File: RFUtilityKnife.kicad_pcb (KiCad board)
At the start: 2 copper layers, 100 x 100 mm, 269 parts, among them J1 Conn_01x01, J10 Conn_01x01, J100 Conn_01x01, J101 Conn_01x01, J11 Conn_01x01, J12 Conn_01x01, J126 Conn_Coaxial, J127 Conn_Coaxial, J128 Conn_01x01, J129 Conn_01x01, J13 Conn_01x01, J130 Conn_01x01, J131 Conn_01x01, J14 Conn_01x01, J15 Conn_01x01, J16 Conn_01x01, J17 Conn_01x01, J18 Conn_Coaxial, J2 Barrel_Jack, J22 Barrel_Jack, J23 Barrel_Jack, J24 Conn_Coaxial, J25 Conn_Coaxial, J26 Conn_01x01, J27 Conn_01x01, J28 Conn_01x01, J29 Conn_01x01, J3 Conn_Coaxial, J30 Conn_01x01, J31 Conn_01x01, J32 Conn_01x01, J33 Conn_01x01, J44 Conn_01x01, J45 Conn_01x01, J48 Conn_01x01, J49 Conn_01x01, J5 Conn_01x01, J53 Conn_01x01, J59 Conn_01x01, J6 Conn_01x01, J60 Conn_01x01, J63 Conn_01x01, J65 Conn_01x01, J7 Conn_01x01, J70 Conn_01x01, J71 Conn_01x01, J72 Conn_01x01, J8 Conn_01x01, J9 Conn_01x01, J93 Conn_Coaxial, J95 Conn_Coaxial, J96 Conn_Coaxial, J98 Conn_01x01, J99 Conn_01x01, Q1 BFP740, Q10 BFP740, Q11 BFP740, Q12 BFP740, Q13 BFP740, Q14 BFP740, Q15 BFP740, Q16 BFP740, Q17 BFP740, Q18 BFP740, Q19 BFP740, Q2 BFP740, Q23 BFP740, Q24 MMBT5551, Q25 MMBT5551, Q26 BFP740, Q27 BFP740, Q28 BFP740, Q3 BFP740, Q4 BFP740, Q5 BFP740, Q6 BFP740, Q7 BFP740, Q9 BFP740, U1 KA78M05_TO252, U2 NE555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

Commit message: Cleaned up the layout
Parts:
- C13: value 10 nF -> 1 nF
- C50, C51, C52: value 15 pF -> 1 pF
- R10, R106, R22, R31, R80, R90: value 22R -> 47R
- R105, R29, R9: value 22R -> 10R
- R2, R43, R44: value 22R -> 100R
- moved C11 17.4 mm to (119.6, 71.5)
- moved JP5 13.4 mm to (109.9, 91.7), turned to 180 degrees
- moved U1 8.40 mm to (118.4, 78.1)
- moved J2 8.27 mm to (111.1, 76.5)
- moved C23 7.58 mm to (116.8, 85.9)
- moved C64 7.57 mm to (116.8, 87.9)
- moved C10 7.21 mm to (113.1, 88.5)
- moved R72 6.87 mm to (73.6, 113.5)
- moved R70 5.81 mm to (72.5, 113.5), turned to 270 degrees
- moved R41 3.41 mm to (73.1, 111.7), turned to 90 degrees
- moved R34 3.23 mm to (144.0, 89.9), turned to 180 degrees
- moved R68 2.95 mm to (150.2, 114.3), turned to 270 degrees
- moved R66 2.95 mm to (149.1, 114.3), turned to 270 degrees
- moved C7 2.66 mm to (144.1, 46.2), turned to 180 degrees
- moved C44 2.63 mm to (70.5, 122.4)
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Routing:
- net GND: track 841.1 -> 987.7 mm, vias 370 -> 454
- net Net-(C16-Pad2): track 75.0 -> 62.5 mm
- net NOISEPOWER: track 119.5 -> 107.8 mm
- net Net-(C10-Pad2): track 24.8 -> 15.7 mm
- net Net-(C39-Pad2): track 11.4 -> 4.74 mm
- net MIXERVCC: track 50.8 -> 54.8 mm
- net Net-(Q16-Pad3): track 8.63 -> 4.70 mm
- net Net-(C38-Pad2): track 5.37 -> 7.62 mm
- net +BATT: track 47.6 -> 49.6 mm
- net Net-(C14-Pad2): track 6.68 -> 8.44 mm
- net Net-(C44-Pad2): track 5.61 -> 7.36 mm
- net HIGHVOLTAGE: track 68.0 -> 69.7 mm
- net Net-(J100-Pad1): track 16.6 -> 15.1 mm
- net Net-(C2-Pad2): track 5.48 -> 6.80 mm
- net Net-(C66-Pad1): track 9.01 -> 10.3 mm
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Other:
- board text added: "NE555"
- board text removed: "LM555"

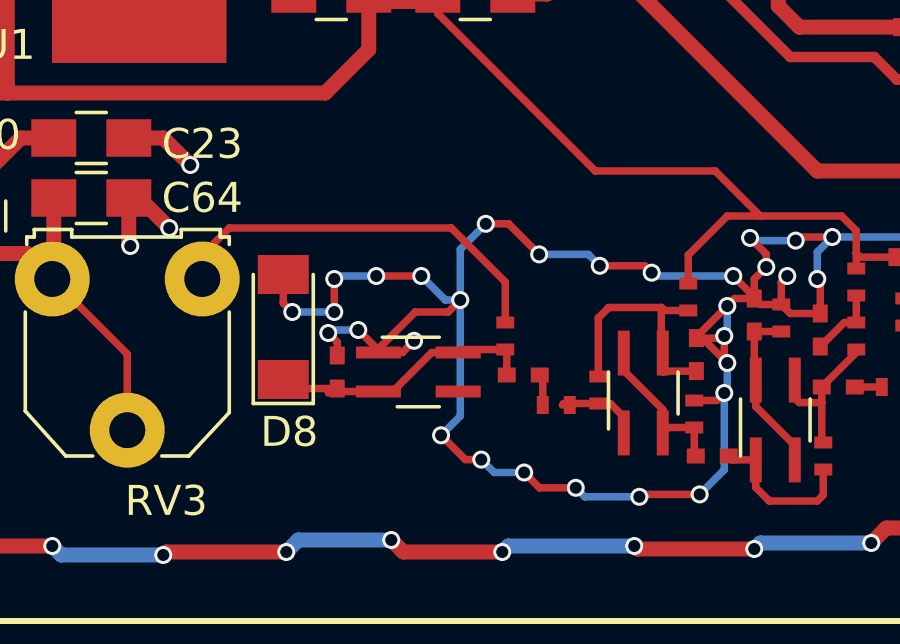
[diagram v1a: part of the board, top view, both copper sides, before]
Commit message: Added vias and changed cut lines
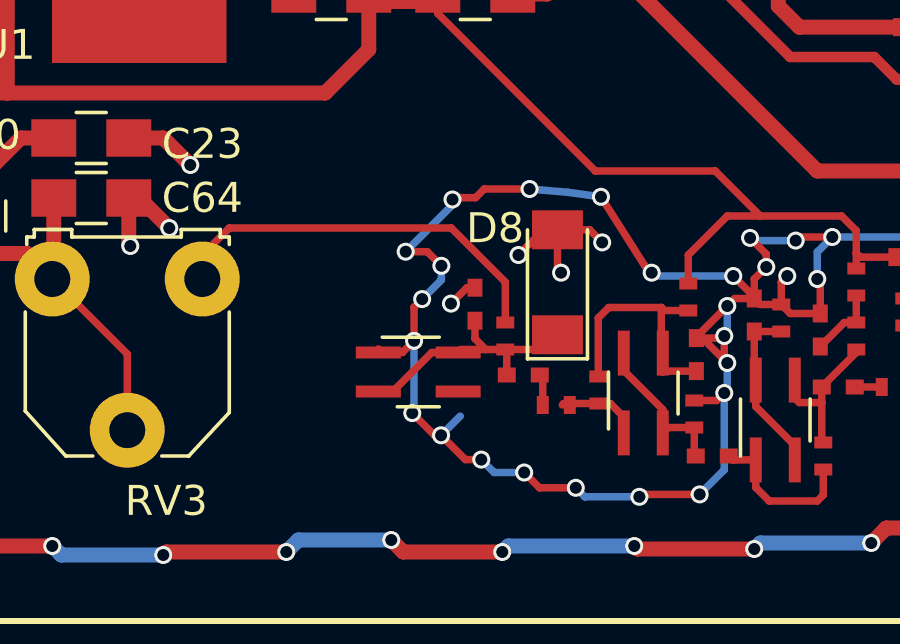
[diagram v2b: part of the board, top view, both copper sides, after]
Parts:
- moved D8 9.26 mm to (132.3, 90.7)
- moved C22 5.12 mm to (129.6, 91.4)
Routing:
- net GND: track 987.7 -> 984.3 mm
